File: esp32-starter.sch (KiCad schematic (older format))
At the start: 35 parts

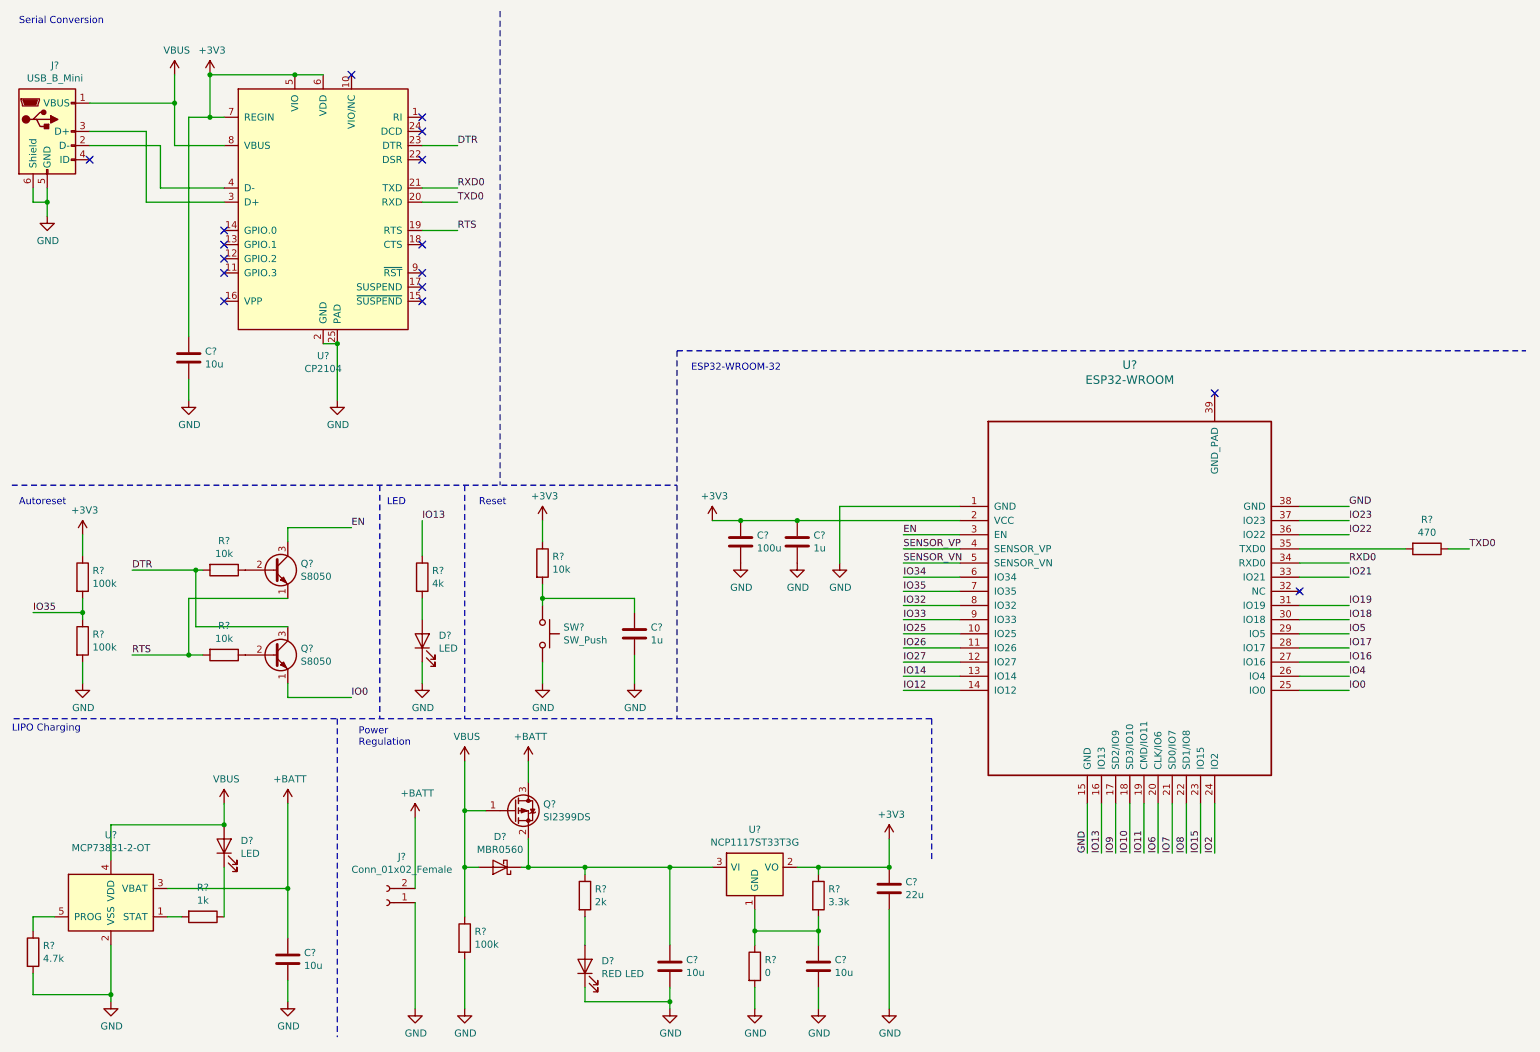
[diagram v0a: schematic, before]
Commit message: fix reset and flash buttons
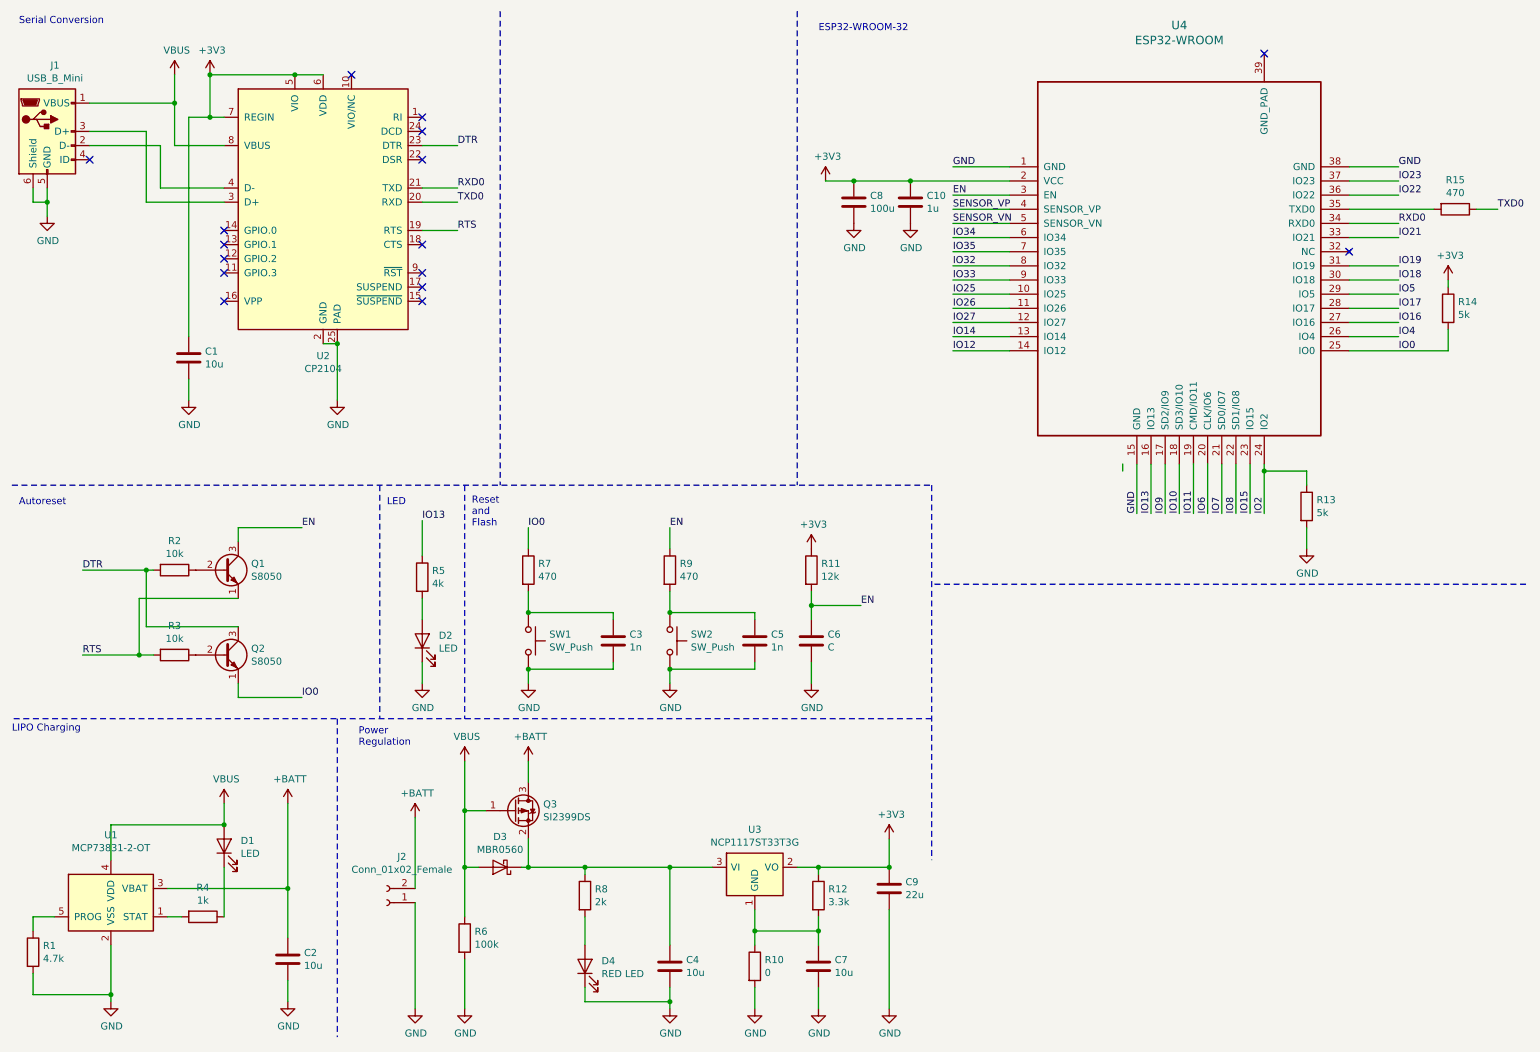
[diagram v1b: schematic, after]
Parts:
- removed C?: 1u, symbol Device:C
- removed R? (x2): 100k, symbol device:R
- removed R?: 10k, symbol device:R
- removed SW?: SW_Push, symbol Switch:SW_Push
- added C3, C5: 1n, symbol Device:C
- added C6: C, symbol Device:C
- added R11: 12k, symbol Device:R
- added R13, R14: 5k, symbol Device:R
- added R7, R9: 470, symbol Device:R
- added SW1, SW2: SW_Push, symbol Switch:SW_Push
- U4: renamed from U?; footprint (none) -> ESP-32:ESP32-WROOM
- gave numbers to parts that had none: 29
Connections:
- net +3V3: now also R11.1, R14.1
- net EN: now also C6.1, R11.2, R9.1
- net GND: now also C3.2, C5.2, C6.2, R13.2, SW1.2, SW2.2
- net IO0: now also R14.2, R7.1
- net IO2: now also R13.1
- new net: C3.1, R7.2, SW1.1
- new net: C5.1, R9.2, SW2.1
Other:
- note added: "Reset\nand\nFlash"
- note removed: "Reset"
- moved on the sheet: C10, C8, Q1, Q2, R15, R2, R3, U4

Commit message: switch to ftdi usb converter
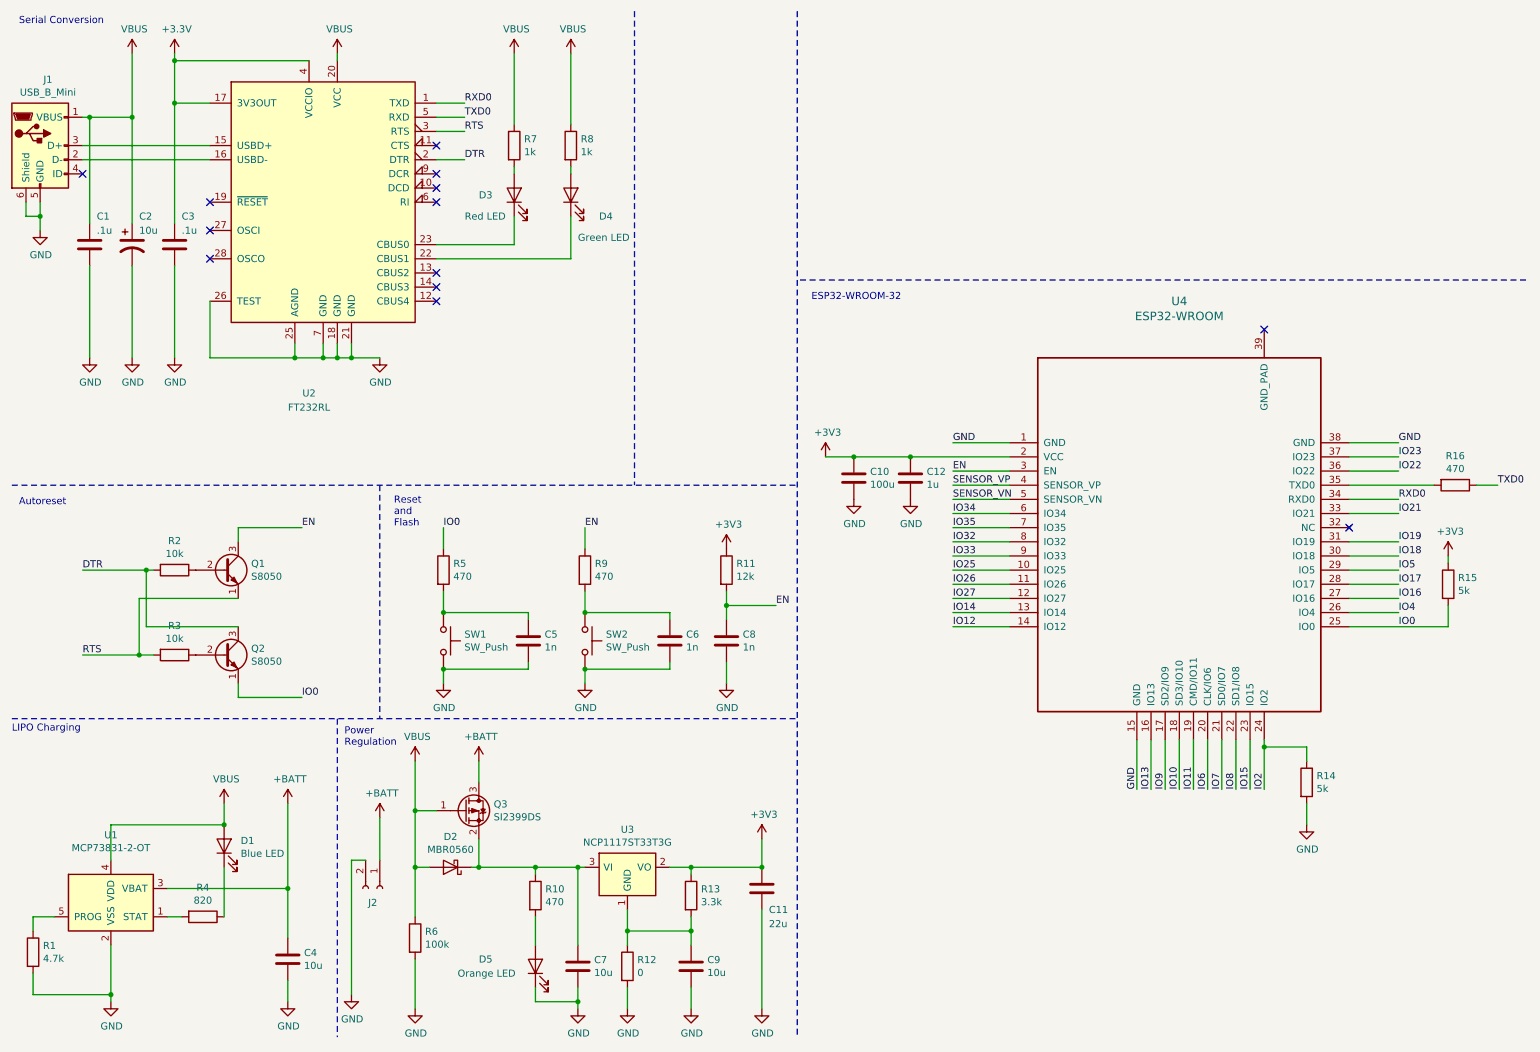
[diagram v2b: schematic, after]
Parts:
- removed D2: LED, symbol Device:LED
- removed R5: 4k, symbol device:R
- removed U2: CP2104, Package_DFN_QFN:QFN-24-1EP_4x4mm_P0.5mm_EP2.6x2.6mm, symbol Interface_USB:CP2104
- added C2: 10u, Capacitor_SMD:C_0805_2012Metric_Pad1.15x1.40mm_HandSolder, symbol Device:CP1
- added C3: .1u, Capacitor_SMD:C_0805_2012Metric_Pad1.15x1.40mm_HandSolder, symbol Device:C
- added D3: Red LED, LED_SMD:LED_0805_2012Metric_Pad1.15x1.40mm_HandSolder, symbol Device:LED
- added D4: Green LED, LED_SMD:LED_0805_2012Metric_Pad1.15x1.40mm_HandSolder, symbol Device:LED
- added R7, R8: 1k, Resistor_SMD:R_0805_2012Metric_Pad1.15x1.40mm_HandSolder, symbol Device:R
- added U2: FT232RL, Package_SO:SSOP-28_5.3x10.2mm_P0.65mm, symbol Interface_USB:FT232RL
- C1: value 10u -> .1u; footprint (none) -> Capacitor_SMD:C_0805_2012Metric_Pad1.15x1.40mm_HandSolder
- C10: renamed from C8; footprint (none) -> Capacitor_SMD:C_0805_2012Metric_Pad1.15x1.40mm_HandSolder
- C11: renamed from C9; footprint (none) -> Capacitor_SMD:C_0805_2012Metric_Pad1.15x1.40mm_HandSolder
- C12: renamed from C10; footprint (none) -> Capacitor_SMD:C_0805_2012Metric_Pad1.15x1.40mm_HandSolder
- C4: renamed from C2; footprint (none) -> Capacitor_SMD:C_0805_2012Metric_Pad1.15x1.40mm_HandSolder
- C5: renamed from C3; footprint (none) -> Capacitor_SMD:C_0805_2012Metric_Pad1.15x1.40mm_HandSolder
- C6: renamed from C5; footprint (none) -> Capacitor_SMD:C_0805_2012Metric_Pad1.15x1.40mm_HandSolder
- C7: renamed from C4; footprint (none) -> Capacitor_SMD:C_0805_2012Metric_Pad1.15x1.40mm_HandSolder
- C8: renamed from C6; value C -> 1n; footprint (none) -> Capacitor_SMD:C_0805_2012Metric_Pad1.15x1.40mm_HandSolder
- C9: renamed from C7; footprint (none) -> Capacitor_SMD:C_0805_2012Metric_Pad1.15x1.40mm_HandSolder
- D1: value LED -> Blue LED; footprint (none) -> LED_SMD:LED_0805_2012Metric_Pad1.15x1.40mm_HandSolder
- D5: renamed from D4; value RED LED -> Orange LED; footprint (none) -> LED_SMD:LED_0805_2012Metric_Pad1.15x1.40mm_HandSolder
- J1: footprint (none) -> Connector_USB:USB_Mini-B_Lumberg_2486_01_Horizontal
- J2: footprint (none) -> Connector_JST:JST_PH_S2B-PH-K_1x02_P2.00mm_Horizontal
- R1, R11, R2, R3, R6, R9: footprint (none) -> Resistor_SMD:R_0805_2012Metric_Pad1.15x1.40mm_HandSolder
- R10: renamed from R8; value 2k -> 470; footprint (none) -> Resistor_SMD:R_0805_2012Metric_Pad1.15x1.40mm_HandSolder
- R12: renamed from R10; footprint (none) -> Resistor_SMD:R_0805_2012Metric_Pad1.15x1.40mm_HandSolder
- R13: renamed from R12; footprint (none) -> Resistor_SMD:R_0805_2012Metric_Pad1.15x1.40mm_HandSolder
- R14: renamed from R13; footprint (none) -> Resistor_SMD:R_0805_2012Metric_Pad1.15x1.40mm_HandSolder
- R15: renamed from R14; footprint (none) -> Resistor_SMD:R_0805_2012Metric_Pad1.15x1.40mm_HandSolder
- R16: renamed from R15; footprint (none) -> Resistor_SMD:R_0805_2012Metric_Pad1.15x1.40mm_HandSolder
- R4: value 1k -> 820; footprint (none) -> Resistor_SMD:R_0805_2012Metric_Pad1.15x1.40mm_HandSolder
- R5: renamed from R7; footprint (none) -> Resistor_SMD:R_0805_2012Metric_Pad1.15x1.40mm_HandSolder
- SW1, SW2: footprint (none) -> Button_Switch_THT:SW_PUSH_6mm
- renumbered D3 to D2
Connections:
- net +3V3: now also C3.1, U2.17 (3V3OUT), U2.4 (VCCIO); no longer C1.1
- net +BATT: now also J2.1 (Pin_1); no longer J2.2 (Pin_2)
- net DTR: now also U2.2 (DTR)
- net GND: now also J2.2 (Pin_2), C2.2, C3.2, U2.18 (GND), U2.21 (GND), U2.25 (AGND), U2.26 (TEST), U2.7 (GND); no longer J2.1 (Pin_1)
- net RTS: now also U2.3 (RTS)
- net RXD0: now also U2.1 (TXD)
- net TXD0: now also U2.5 (RXD)
- net VBUS: now also C1.1, C2.1, R7.1, R8.1, U2.20 (VCC)
- net at J1.3 (D+): now also U2.15 (USBD+)
- net at J1.2 (D-): now also U2.16 (USBD-)
- new net: D4.1 (K), U2.22 (CBUS1)
- new net: D3.1 (K), U2.23 (CBUS0)
- new net: D3.2 (A), R7.2
- new net: D4.2 (A), R8.2
- no-connect marks 16 -> 13
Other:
- note removed: "LED"
- moved on the sheet: C10, C11, C12, C5, C6, C7, C8, C9, D2, D5, J1, J2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
